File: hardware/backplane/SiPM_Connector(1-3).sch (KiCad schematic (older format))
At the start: 8 parts, among them J101 Conn_02x34_Odd_Even, J102 ERF8-060-05.0-L-DV, J103 Conn_02x34_Odd_Even, J201 Conn_02x34_Odd_Even-Connector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, J203 Conn_02x34_Odd_Even-Connector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, J301 Conn_02x34_Odd_Even-Connector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, J302 ERF8-060-05.0-L-DV, J303 Conn_02x34_Odd_Even-Connector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

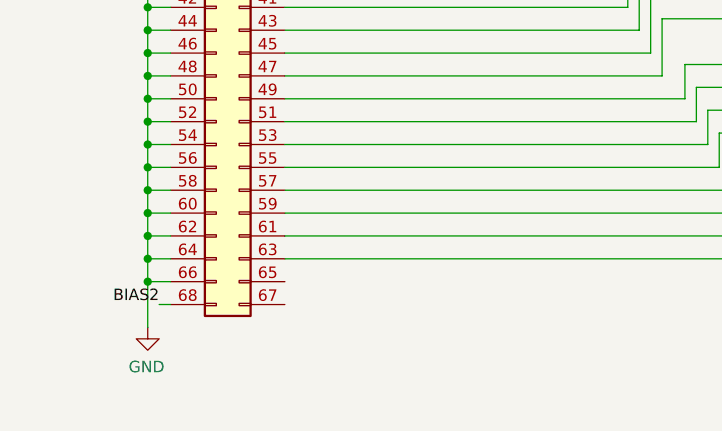
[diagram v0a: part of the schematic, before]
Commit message: Readout_FMC started
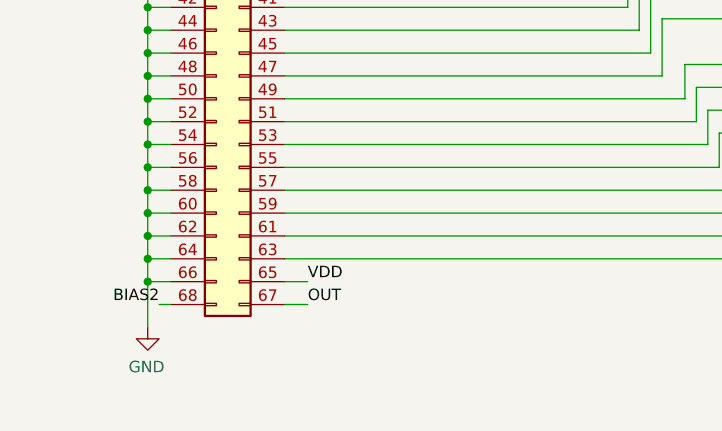
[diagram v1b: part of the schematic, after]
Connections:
- net OUT: now also J301.67 (Pin_67)
- net VDD: now also J301.65 (Pin_65)
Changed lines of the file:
@@
 Wire Wire Line
 	2050 4050 2050 4150
-Connection ~ 2050 4150
-Wire Wire Line
-	2050 4150 2050 4350
-$Comp
-L backplane-prototype-rescue:GND-power #PWR01
-U 1 1 63C5DEA9
-P 2050 4350
-F 0 "#PWR01" H 2050 4100 50  0001 C CNN
-F 1 "GND" H 2055 4177 50  0000 C CNN
-F 2 "" H 2050 4350 50  0001 C CNN
-F 3 "" H 2050 4350 50  0001 C CNN
-	1    2050 4350
-	-1   0    0    -1
-$EndComp
 Wire Wire Line
 	2150 950  2050 950
-Wire Wire Line
-	2150 4250 2100 4250
 Text Label 2050 950  2    50   ~ 0
 BIAS1
-Text Label 2100 4250 2    50   ~ 0
-BIAS2
 Text Label 2750 950  0    50   ~ 0
 CH0
@@
 Connection ~ 4900 13000
 Wire Wire Line
-	4900 13000 4900 13500
-Wire Wire Line
 	6000 13000 6100 13000
 Connection ~ 6100 13000
@@
 Wire Wire Line
 	2050 8600 2050 8700
-Connection ~ 2050 8700
-Wire Wire Line
-	2050 8700 2050 8900
-$Comp
-L backplane-prototype-rescue:GND-power #PWR?
-U 1 1 63C5DEB1
-P 2050 8900
-F 0 "#PWR?" H 2050 8650 50  0001 C CNN
-F 1 "GND" H 2055 8727 50  0000 C CNN
-F 2 "" H 2050 8900 50  0001 C CNN
-F 3 "" H 2050 8900 50  0001 C CNN
-	1    2050 8900
-	-1   0    0    -1
-$EndComp
-Wire Wire Line
-	2150 5500 2050 5500
-Wire Wire Line
-	2150 8800 2100 8800
-Text Label 2050 5500 2    50   ~ 0
-BIAS1
-Text Label 2100 8800 2    50   ~ 0
-BIAS2
 Wire Wire Line
 	2150 10050 2050 10050
@@
 Wire Wire Line
 	2050 13050 2050 13150
-Connection ~ 2050 13150
-Wire Wire Line
-	2050 13150 2050 13350
-$Comp
-L backplane-prototype-rescue:GND-power #PWR?
-U 1 1 63C5DEB2
-P 2050 13350
-F 0 "#PWR?" H 2050 13100 50  0001 C CNN
-F 1 "GND" H 2055 13177 50  0000 C CNN
-F 2 "" H 2050 13350 50  0001 C CNN
-F 3 "" H 2050 13350 50  0001 C CNN
-	1    2050 13350
-	-1   0    0    -1
-$EndComp
-Wire Wire Line
-	2150 9950 2050 9950
-Wire Wire Line
-	2150 13250 2100 13250
-Text Label 2050 9950 2    50   ~ 0
-BIAS1
-Text Label 2100 13250 2    50   ~ 0
-BIAS2
 Wire Wire Line
 	8850 5600 8950 5600
@@
 	8950 8700 8950 8900
 $Comp
-L backplane-prototype-rescue:GND-power #PWR?
+L backplane-prototype-rescue:GND-power #PWR0103
 U 1 1 63C5DEB3
 P 8950 8900
-F 0 "#PWR?" H 8950 8650 50  0001 C CNN
+F 0 "#PWR0103" H 8950 8650 50  0001 C CNN
 F 1 "GND" H 8955 8727 50  0000 C CNN
 F 2 "" H 8950 8900 50  0001 C CNN
@@
 	8950 13150 8950 13350
 $Comp
-L backplane-prototype-rescue:GND-power #PWR?
+L backplane-prototype-rescue:GND-power #PWR0104
 U 1 1 63C5DEB4
 P 8950 13350
-F 0 "#PWR?" H 8950 13100 50  0001 C CNN
+F 0 "#PWR0104" H 8950 13100 50  0001 C CNN
 F 1 "GND" H 8955 13177 50  0000 C CNN
 F 2 "" H 8950 13350 50  0001 C CNN
@@
 Wire Wire Line
 	8900 8800 8900 8900
+Wire Wire Line
+	4900 13000 4900 13500
+Wire Wire Line
+	2150 13250 2100 13250
+Text Label 2100 13250 2    50   ~ 0
+BIAS2
+Connection ~ 2050 13150
+$Comp
+L backplane-prototype-rescue:GND-power #PWR0105
+U 1 1 63C5DEB2
+P 2050 13350
+F 0 "#PWR0105" H 2050 13100 50  0001 C CNN
+F 1 "GND" H 2055 13177 50  0000 C CNN
+F 2 "" H 2050 13350 50  0001 C CNN
+F 3 "" H 2050 13350 50  0001 C CNN
+	1    2050 13350
+	-1   0    0    -1
+$EndComp
+Wire Wire Line
+	2050 13150 2050 13350
+Wire Wire Line
+	2150 9950 2050 9950
+Text Label 2050 9950 2    50   ~ 0
+BIAS1
+Connection ~ 2050 8700
+$Comp
+L backplane-prototype-rescue:GND-power #PWR0106
+U 1 1 63C5DEB1
+P 2050 8900
+F 0 "#PWR0106" H 2050 8650 50  0001 C CNN
+F 1 "GND" H 2055 8727 50  0000 C CNN
+F 2 "" H 2050 8900 50  0001 C CNN
+F 3 "" H 2050 8900 50  0001 C CNN
+	1    2050 8900
+	-1   0    0    -1
+$EndComp
+Wire Wire Line
+	2050 8700 2050 8900
+Wire Wire Line
+	2150 8800 2100 8800
+Text Label 2100 8800 2    50   ~ 0
+BIAS2
+Wire Wire Line
+	2150 4250 2100 4250
+Text Label 2100 4250 2    50   ~ 0
+BIAS2
+Connection ~ 2050 4150
+$Comp
+L backplane-prototype-rescue:GND-power #PWR01
+U 1 1 63C5DEA9
+P 2050 4350
+F 0 "#PWR01" H 2050 4100 50  0001 C CNN
+F 1 "GND" H 2055 4177 50  0000 C CNN
+F 2 "" H 2050 4350 50  0001 C CNN
+F 3 "" H 2050 4350 50  0001 C CNN
+	1    2050 4350
+	-1   0    0    -1
+$EndComp
+Wire Wire Line
+	2050 4150 2050 4350
+Wire Wire Line
+	2150 5500 2050 5500
+Text Label 2050 5500 2    50   ~ 0
+BIAS1
+Text Label 2750 13150 0    50   ~ 0
+VDD
+Text Label 2750 13250 0    50   ~ 0
+OUT
+Wire Wire Line
+	2750 13250 2650 13250
+Wire Wire Line
+	2750 13150 2650 13150
 $EndSCHEMATC

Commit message: Backplane Layout Started
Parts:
- removed J201, J203, J303: Conn_02x34_Odd_Even-Connector_Generic, symbol backplane-prototype-rescue:Conn_02x34_Odd_Even-Connector_Generic
- added J201, J203, J303: Conn_02x34_Odd_Even-Connector_Generic, backplane:SAMTEC_CLM-134-02-F-D, symbol backplane-rescue:Conn_02x34_Odd_Even-Connector_Generic-backplane-prototype-resc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
- J101, J103: footprint Backplane-prototype:SAMTEC_CLM-134-02-F-D -> backplane:SAMTEC_CLM-134-02-F-D; symbol backplane-prototype-rescue:Conn_02x34_Odd_Even-Connector_Generic -> backplane-rescue:Conn_02x34_Odd_Even-Connector_Generic-backplane-prototype-rescue
- J102, J302: footprint Backplane-prototype:ERF8-060-05.0-L-DV -> backplane:ERF8-060-05.0-L-DV; symbol backplane-prototype-rescue:ERF8-060-XX.X-X-DV-ERF8-060-05.0-L-DV -> backplane-rescue:ERF8-060-XX.X-X-DV-ERF8-060-05.0-L-DV-backplane-prototype-rescue
- J301: footprint (none) -> backplane:SAMTEC_CLM-134-02-F-D; symbol backplane-prototype-rescue:Conn_02x34_Odd_Even-Connector_Generic -> backplane-rescue:Conn_02x34_Odd_Even-Connector_Generic-backplane-prototype-rescue
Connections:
- net BCH0: now also J103.67 (Pin_67); no longer J103.1 (Pin_1)
- net BCH1: now also J103.65 (Pin_65); no longer J103.3 (Pin_3)
- net BCH10: now also J103.47 (Pin_47); no longer J103.21 (Pin_21)
- net BCH11: now also J103.45 (Pin_45); no longer J103.23 (Pin_23)
- net BCH12: now also J103.43 (Pin_43); no longer J103.25 (Pin_25)
- net BCH13: now also J103.41 (Pin_41); no longer J103.27 (Pin_27)
- net BCH14: now also J103.39 (Pin_39); no longer J103.29 (Pin_29)
- net BCH15: now also J103.37 (Pin_37); no longer J103.31 (Pin_31)
- net BCH16: now also J103.35 (Pin_35); no longer J103.33 (Pin_33)
- net BCH17: now also J103.33 (Pin_33); no longer J103.35 (Pin_35)
- net BCH18: now also J103.31 (Pin_31); no longer J103.37 (Pin_37)
- net BCH19: now also J103.29 (Pin_29); no longer J103.39 (Pin_39)
- net BCH2: now also J103.63 (Pin_63); no longer J103.5 (Pin_5)
- net BCH20: now also J103.27 (Pin_27); no longer J103.41 (Pin_41)
- net BCH21: now also J103.25 (Pin_25); no longer J103.43 (Pin_43)
- net BCH22: now also J103.23 (Pin_23); no longer J103.45 (Pin_45)
- net BCH23: now also J103.21 (Pin_21); no longer J103.47 (Pin_47)
- net BCH24: now also J103.19 (Pin_19); no longer J103.49 (Pin_49)
- net BCH25: now also J103.17 (Pin_17); no longer J103.51 (Pin_51)
- net BCH26: now also J103.15 (Pin_15); no longer J103.53 (Pin_53)
- net BCH27: now also J103.13 (Pin_13); no longer J103.55 (Pin_55)
- net BCH28: now also J103.11 (Pin_11); no longer J103.57 (Pin_57)
- net BCH29: now also J103.9 (Pin_9); no longer J103.59 (Pin_59)
- net BCH3: now also J103.61 (Pin_61); no longer J103.7 (Pin_7)
- net BCH30: now also J103.7 (Pin_7); no longer J103.61 (Pin_61)
- net BCH31: now also J103.5 (Pin_5); no longer J103.63 (Pin_63)
- net BCH4: now also J103.59 (Pin_59); no longer J103.9 (Pin_9)
- net BCH5: now also J103.57 (Pin_57); no longer J103.11 (Pin_11)
- net BCH6: now also J103.55 (Pin_55); no longer J103.13 (Pin_13)
- net BCH7: now also J103.53 (Pin_53); no longer J103.15 (Pin_15)
- net BCH8: now also J103.51 (Pin_51); no longer J103.17 (Pin_17)
- net BCH9: now also J103.49 (Pin_49); no longer J103.19 (Pin_19)
- net BIAS1: now also J201.2 (Pin_2)
- net BIAS2: now also J201.68 (Pin_68)
- net BIAS3: now also J103.68 (Pin_68), J203.68 (Pin_68), J303.68 (Pin_68); no longer J103.2 (Pin_2)
- net BIAS4: now also J103.2 (Pin_2), J203.2 (Pin_2), J303.2 (Pin_2); no longer J103.67 (Pin_67), J103.68 (Pin_68)
- net CH0: no longer J102.84
- net CH1: no longer J102.86
- net CH10: no longer J102.106
- net CH11: no longer J102.108
- net CH12: no longer J102.110
- net CH13: no longer J102.112
- net CH14: no longer J102.114
- net CH15: no longer J102.116
- net CH16: no longer J102.120
- net CH17: no longer J302.2
- net CH18: no longer J302.4
- net CH19: no longer J302.6
- net CH2: no longer J102.88
- net CH20: no longer J302.8
- net CH21: no longer J302.10
- net CH22: no longer J302.12
- net CH23: no longer J302.14
- net CH24: no longer J302.18
- net CH25: no longer J302.20
- net CH26: no longer J302.22
- net CH27: no longer J302.24
- net CH28: no longer J302.26
- net CH29: no longer J302.28
- net CH3: no longer J102.90
- net CH30: no longer J302.30
- net CH31: no longer J302.32
- net CH4: no longer J102.92
- net CH5: no longer J102.94
- net CH6: no longer J102.96
- net CH7: no longer J102.98
- net CH8: no longer J102.102
- net CH9: no longer J102.104
- net GND: now also J201.10 (Pin_10), J201.12 (Pin_12), J201.14 (Pin_14), J201.16 (Pin_16), J201.18 (Pin_18), J201.20 (Pin_20), J201.22 (Pin_22), J201.24 (Pin_24), J201.26 (Pin_26), J201.28 (Pin_28), J201.30 (Pin_30), J201.32 (Pin_32), J201.34 (Pin_34), J201.36 (Pin_36), J201.38 (Pin_38), J201.4 (Pin_4), J201.40 (Pin_40), J201.42 (Pin_42), J201.44 (Pin_44), J201.46 (Pin_46), J201.48 (Pin_48), J201.50 (Pin_50), J201.52 (Pin_52), J201.54 (Pin_54), J201.56 (Pin_56), J201.58 (Pin_58), J201.6 (Pin_6), J201.60 (Pin_60), J201.62 (Pin_62), J201.64 (Pin_64), J201.66 (Pin_66), J201.8 (Pin_8), J203.10 (Pin_10), J203.12 (Pin_12), J203.14 (Pin_14), J203.16 (Pin_16), J203.18 (Pin_18), J203.20 (Pin_20), J203.22 (Pin_22), J203.24 (Pin_24), J203.26 (Pin_26), J203.28 (Pin_28), J203.30 (Pin_30), J203.32 (Pin_32), J203.34 (Pin_34), J203.36 (Pin_36), J203.38 (Pin_38), J203.4 (Pin_4), J203.40 (Pin_40), J203.42 (Pin_42), J203.44 (Pin_44), J203.46 (Pin_46), J203.48 (Pin_48), J203.50 (Pin_50), J203.52 (Pin_52), J203.54 (Pin_54), J203.56 (Pin_56), J203.58 (Pin_58), J203.6 (Pin_6), J203.60 (Pin_60), J203.62 (Pin_62), J203.64 (Pin_64), J203.66 (Pin_66), J203.8 (Pin_8), J303.10 (Pin_10), J303.12 (Pin_12), J303.14 (Pin_14), J303.16 (Pin_16), J303.18 (Pin_18), J303.20 (Pin_20), J303.22 (Pin_22), J303.24 (Pin_24), J303.26 (Pin_26), J303.28 (Pin_28), J303.30 (Pin_30), J303.32 (Pin_32), J303.34 (Pin_34), J303.36 (Pin_36), J303.38 (Pin_38), J303.4 (Pin_4), J303.40 (Pin_40), J303.42 (Pin_42), J303.44 (Pin_44), J303.46 (Pin_46), J303.48 (Pin_48), J303.50 (Pin_50), J303.52 (Pin_52), J303.54 (Pin_54), J303.56 (Pin_56), J303.58 (Pin_58), J303.6 (Pin_6), J303.60 (Pin_60), J303.62 (Pin_62), J303.64 (Pin_64), J303.66 (Pin_66), J303.8 (Pin_8)
- net OUT: now also J201.67 (Pin_67)
- net VDD: now also J201.65 (Pin_65)
- net BCH32: now reaches J102.83
- net BCH32: now also J203.67 (Pin_67)
- net BCH37: now reaches J102.93
- net BCH37: now also J203.57 (Pin_57)
- net BCH38: now reaches J102.95
- net BCH38: now also J203.55 (Pin_55)
- net BCH39: now reaches J102.97
- net BCH39: now also J203.53 (Pin_53)
- net BCH40: now reaches J102.101
- net BCH40: now also J203.51 (Pin_51)
- net BCH41: now reaches J102.103
- net BCH41: now also J203.49 (Pin_49)
- net BCH42: now reaches J102.105
- net BCH42: now also J203.47 (Pin_47)
- net BCH43: now reaches J102.107
- net BCH43: now also J203.45 (Pin_45)
- net BCH44: now reaches J102.109
- net BCH44: now also J203.43 (Pin_43)
- net BCH45: now reaches J102.111
- net BCH45: now also J203.41 (Pin_41)
- net BCH46: now reaches J102.113
- net BCH46: now also J203.39 (Pin_39)
- net BCH33: now reaches J102.85
- net BCH33: now also J203.65 (Pin_65)
- net BCH47: now reaches J102.115
- net BCH47: now also J203.37 (Pin_37)
- net BCH48: now reaches J102.119
- net BCH48: now also J203.35 (Pin_35)
- net BCH49: now reaches J302.1
- net BCH49: now also J203.33 (Pin_33)
- net BCH50: now reaches J302.3
- net BCH50: now also J203.31 (Pin_31)
- net BCH51: now reaches J302.5
- net BCH51: now also J203.29 (Pin_29)
- net BCH52: now reaches J302.7
- net BCH52: now also J203.27 (Pin_27)
- net BCH53: now reaches J302.9
- net BCH53: now also J203.25 (Pin_25)
- net BCH54: now reaches J302.11
- net BCH54: now also J203.23 (Pin_23)
- net BCH55: now reaches J302.13
- net BCH55: now also J203.21 (Pin_21)
- net BCH56: now reaches J302.17
- net BCH56: now also J203.19 (Pin_19)
- net BCH34: now reaches J102.87
- net BCH34: now also J203.63 (Pin_63)
- net BCH57: now reaches J302.19
- net BCH57: now also J203.17 (Pin_17)
- net BCH58: now reaches J302.21
- net BCH58: now also J203.15 (Pin_15)
- net BCH59: now reaches J302.23
- net BCH59: now also J203.13 (Pin_13)
- net BCH60: now reaches J302.25
- net BCH60: now also J203.11 (Pin_11)
- net BCH61: now reaches J302.27
- net BCH61: now also J203.9 (Pin_9)
- net BCH62: now reaches J302.29
- net BCH62: now also J203.7 (Pin_7)
- net BCH63: now reaches J302.31
- net BCH63: now also J203.5 (Pin_5)
- net BCH35: now reaches J102.89
- net BCH35: now also J203.61 (Pin_61)
- net BCH36: now reaches J102.91
- net BCH36: now also J203.59 (Pin_59)
- net CH89: now reaches J301.51 (Pin_51), J302.100
- net BCH90: now reaches J302.101
- net BCH90: now also J303.15 (Pin_15)
- net CH90: now reaches J301.53 (Pin_53), J302.102
- net BCH91: now reaches J302.103
- net BCH91: now also J303.13 (Pin_13)
- net CH91: now reaches J301.55 (Pin_55), J302.104
- net BCH92: now reaches J302.105
- net BCH92: now also J303.11 (Pin_11)
- net CH92: now reaches J301.57 (Pin_57), J302.106
- net BCH93: now reaches J302.107
- net BCH93: now also J303.9 (Pin_9)
- net CH93: now reaches J301.59 (Pin_59), J302.108
- net BCH94: now reaches J302.109
- net BCH94: now also J303.7 (Pin_7)
- net CH94: now reaches J301.61 (Pin_61), J302.110
- net BCH95: now reaches J302.111
- net BCH95: now also J303.5 (Pin_5)
- net CH95: now reaches J301.63 (Pin_63), J302.112
- net BCH64: now reaches J302.43
- net BCH64: now also J303.67 (Pin_67)
- net CH64: now reaches J301.1 (Pin_1), J302.44
- net BCH65: now reaches J302.45
- net BCH65: now also J303.65 (Pin_65)
- net CH65: now reaches J301.3 (Pin_3), J302.46
- net BCH66: now reaches J302.47
- net BCH66: now also J303.63 (Pin_63)
- net CH66: now reaches J301.5 (Pin_5), J302.48
- net BCH67: now reaches J302.49
- net BCH67: now also J303.61 (Pin_61)
- net CH67: now reaches J301.7 (Pin_7), J302.50
- net BCH68: now reaches J302.51
- net BCH68: now also J303.59 (Pin_59)
- net CH68: now reaches J301.9 (Pin_9), J302.52
- net BCH69: now reaches J302.53
- net BCH69: now also J303.57 (Pin_57)
- net CH69: now reaches J301.11 (Pin_11), J302.54
- net BCH70: now reaches J302.55
- net BCH70: now also J303.55 (Pin_55)
- net CH70: now reaches J301.13 (Pin_13), J302.56
- net BCH71: now reaches J302.57
- net BCH71: now also J303.53 (Pin_53)
- net CH71: now reaches J301.15 (Pin_15), J302.58
- net BCH72: now reaches J302.61
- net BCH72: now also J303.51 (Pin_51)
- net CH72: now reaches J301.17 (Pin_17), J302.62
- net BCH73: now reaches J302.63
- net BCH73: now also J303.49 (Pin_49)
- net CH73: now reaches J301.19 (Pin_19), J302.64
- net BCH74: now reaches J302.65
- net BCH74: now also J303.47 (Pin_47)
- net CH74: now reaches J301.21 (Pin_21), J302.66
- net BCH75: now reaches J302.67
- net BCH75: now also J303.45 (Pin_45)
- net CH75: now reaches J301.23 (Pin_23), J302.68
- net BCH76: now reaches J302.69
- net BCH76: now also J303.43 (Pin_43)
- net CH76: now reaches J301.25 (Pin_25), J302.70
- net BCH77: now reaches J302.71
- net BCH77: now also J303.41 (Pin_41)
- net CH77: now reaches J301.27 (Pin_27), J302.72
- net BCH78: now reaches J302.73
- net BCH78: now also J303.39 (Pin_39)
- net CH78: now reaches J301.29 (Pin_29), J302.74
- net BCH79: now reaches J302.75
- net BCH79: now also J303.37 (Pin_37)
- net CH79: now reaches J301.31 (Pin_31), J302.76
- net BCH80: now reaches J302.79
- net BCH80: now also J303.35 (Pin_35)
- net CH80: now reaches J301.33 (Pin_33), J302.80
- net BCH81: now reaches J302.81
- net BCH81: now also J303.33 (Pin_33)
- net CH81: now reaches J301.35 (Pin_35), J302.82
- net BCH82: now reaches J302.83
- net BCH82: now also J303.31 (Pin_31)
- net CH82: now reaches J301.37 (Pin_37), J302.84
- net BCH83: now reaches J302.85
- net BCH83: now also J303.29 (Pin_29)
- net CH83: now reaches J301.39 (Pin_39), J302.86
- net BCH84: now reaches J302.87
- net BCH84: now also J303.27 (Pin_27)
- net CH84: now reaches J301.41 (Pin_41), J302.88
- net BCH85: now reaches J302.89
- net BCH85: now also J303.25 (Pin_25)
- net CH85: now reaches J301.43 (Pin_43), J302.90
- net BCH86: now reaches J302.91
- net BCH86: now also J303.23 (Pin_23)
- net CH86: now reaches J301.45 (Pin_45), J302.92
- net BCH87: now reaches J302.93
- net BCH87: now also J303.21 (Pin_21)
- net CH87: now reaches J301.47 (Pin_47), J302.94
- net BCH88: now reaches J302.97
- net BCH88: now also J303.19 (Pin_19)
- net CH88: now reaches J301.49 (Pin_49), J302.98
- net BCH89: now reaches J302.99
- net BCH89: now also J303.17 (Pin_17)
- new net CH32: J102.84, J201.1 (Pin_1)
- new net CH33: J102.86, J201.3 (Pin_3)
- new net CH34: J102.88, J201.5 (Pin_5)
- new net CH35: J102.90, J201.7 (Pin_7)
- new net CH36: J102.92, J201.9 (Pin_9)
- new net CH37: J102.94, J201.11 (Pin_11)
- new net CH38: J102.96, J201.13 (Pin_13)
- new net CH39: J102.98, J201.15 (Pin_15)
- new net CH40: J102.102, J201.17 (Pin_17)
- new net CH41: J102.104, J201.19 (Pin_19)
- new net CH42: J102.106, J201.21 (Pin_21)
- new net CH43: J102.108, J201.23 (Pin_23)
- new net CH44: J102.110, J201.25 (Pin_25)
- new net CH45: J102.112, J201.27 (Pin_27)
- new net CH46: J102.114, J201.29 (Pin_29)
- new net CH47: J102.116, J201.31 (Pin_31)
- new net CH48: J102.120, J201.33 (Pin_33)
- new net CH49: J201.35 (Pin_35), J302.2
- new net CH50: J201.37 (Pin_37), J302.4
- new net CH51: J201.39 (Pin_39), J302.6
- new net CH52: J201.41 (Pin_41), J302.8
- new net CH53: J201.43 (Pin_43), J302.10
- new net CH54: J201.45 (Pin_45), J302.12
- new net CH55: J201.47 (Pin_47), J302.14
- new net CH56: J201.49 (Pin_49), J302.18
- new net CH57: J201.51 (Pin_51), J302.20
- new net CH58: J201.53 (Pin_53), J302.22
- new net CH59: J201.55 (Pin_55), J302.24
- new net CH60: J201.57 (Pin_57), J302.26
- new net CH61: J201.59 (Pin_59), J302.28
- new net CH62: J201.61 (Pin_61), J302.30
- new net CH63: J201.63 (Pin_63), J302.32
- no-connect marks 3 -> 6
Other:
- moved on the sheet: J101, J102, J103, J301, J302
